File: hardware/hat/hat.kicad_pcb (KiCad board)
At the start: 4 copper layers, 65 x 56 mm, 82 parts, among them J1 GPIO, J2 Uart, J3 LineIn, J4 LineOut, J5 Headphone, U1 CAT24C256, U2 TPS7A20xxxDBV, U3 Oled, U4 MAX98089ETN_T, Y1 12.288MHz

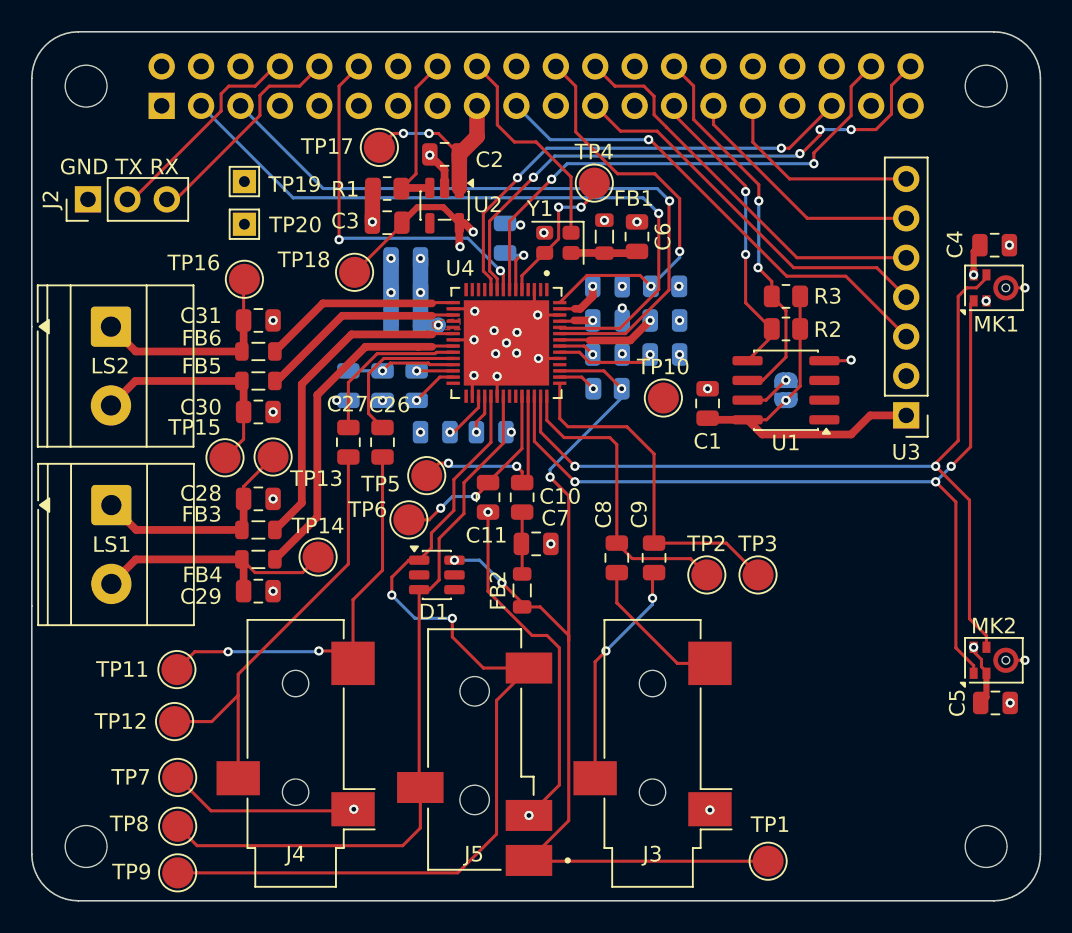
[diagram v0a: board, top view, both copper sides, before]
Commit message: make hat 100 x sheetnum
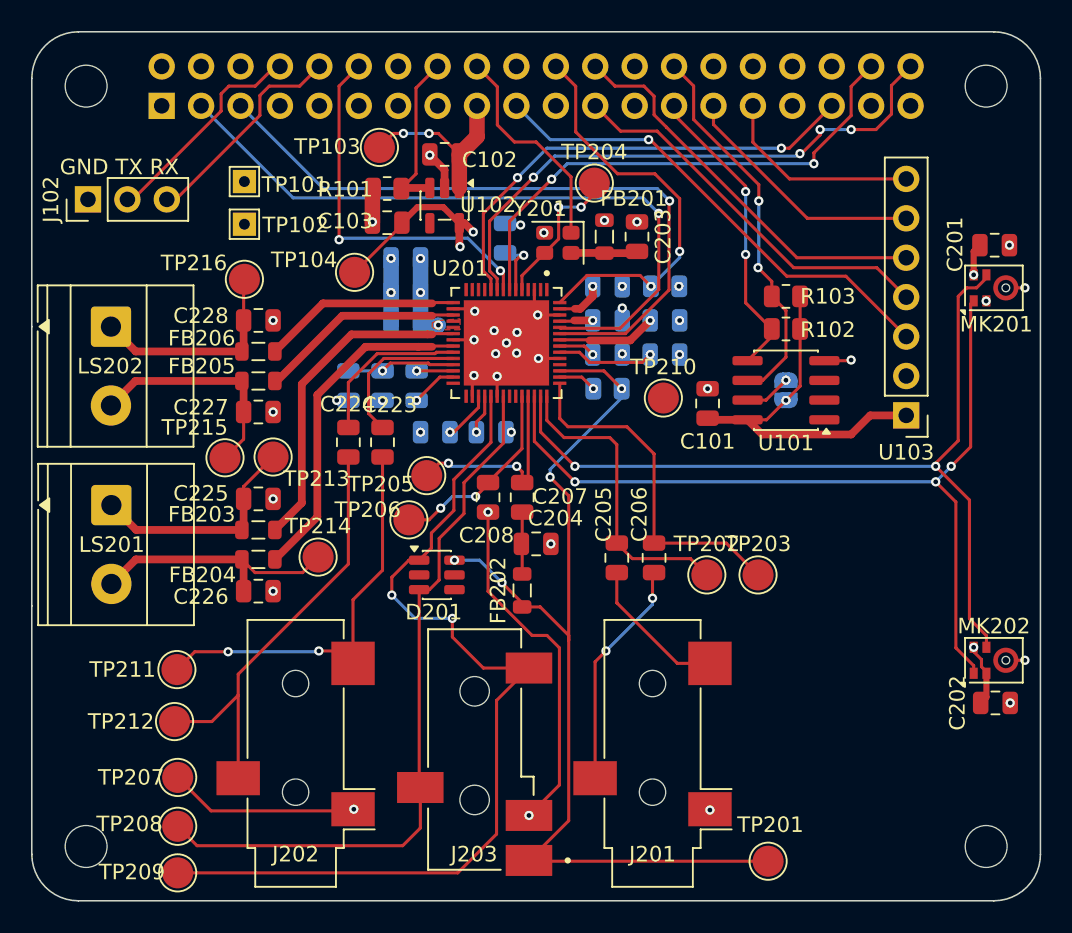
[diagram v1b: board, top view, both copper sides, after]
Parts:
- renumbered C1 to C101, C2 to C102, C3 to C103, C4 to C201, C5 to C202, C6 to C203, C7 to C204, C8 to C205, C9 to C206, C10 to C207, C11 to C208, C12 to C209, C13 to C210, C14 to C211, C15 to C212, C16 to C213, C17 to C214, C18 to C215, C19 to C216, C20 to C217, C21 to C218, C22 to C219, C23 to C220, C24 to C221, C25 to C222, C26 to C223, C27 to C224, C28 to C225, C29 to C226, C30 to C227, C31 to C228, D1 to D201, FB1 to FB201, FB2 to FB202, FB3 to FB203, FB4 to FB204, FB5 to FB205, FB6 to FB206, J1 to J101, J2 to J102, J3 to J201, J4 to J202, J5 to J203, JP1 to JP101, LS1 to LS201, LS2 to LS202, MK1 to MK201, MK2 to MK202, R1 to R101, R2 to R102, R3 to R103, R4 to R201, R5 to R202, TP19 to TP101, TP20 to TP102, TP17 to TP103, TP18 to TP104, TP1 to TP201, TP2 to TP202, TP3 to TP203, TP4 to TP204, TP5 to TP205, TP6 to TP206, TP7 to TP207, TP8 to TP208, TP9 to TP209, TP10 to TP210, TP11 to TP211, TP12 to TP212, TP13 to TP213, TP14 to TP214, TP15 to TP215, TP16 to TP216, U1 to U101, U2 to U102, U3 to U103, U4 to U201, Y1 to Y201

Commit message: move ldo into audio sheet
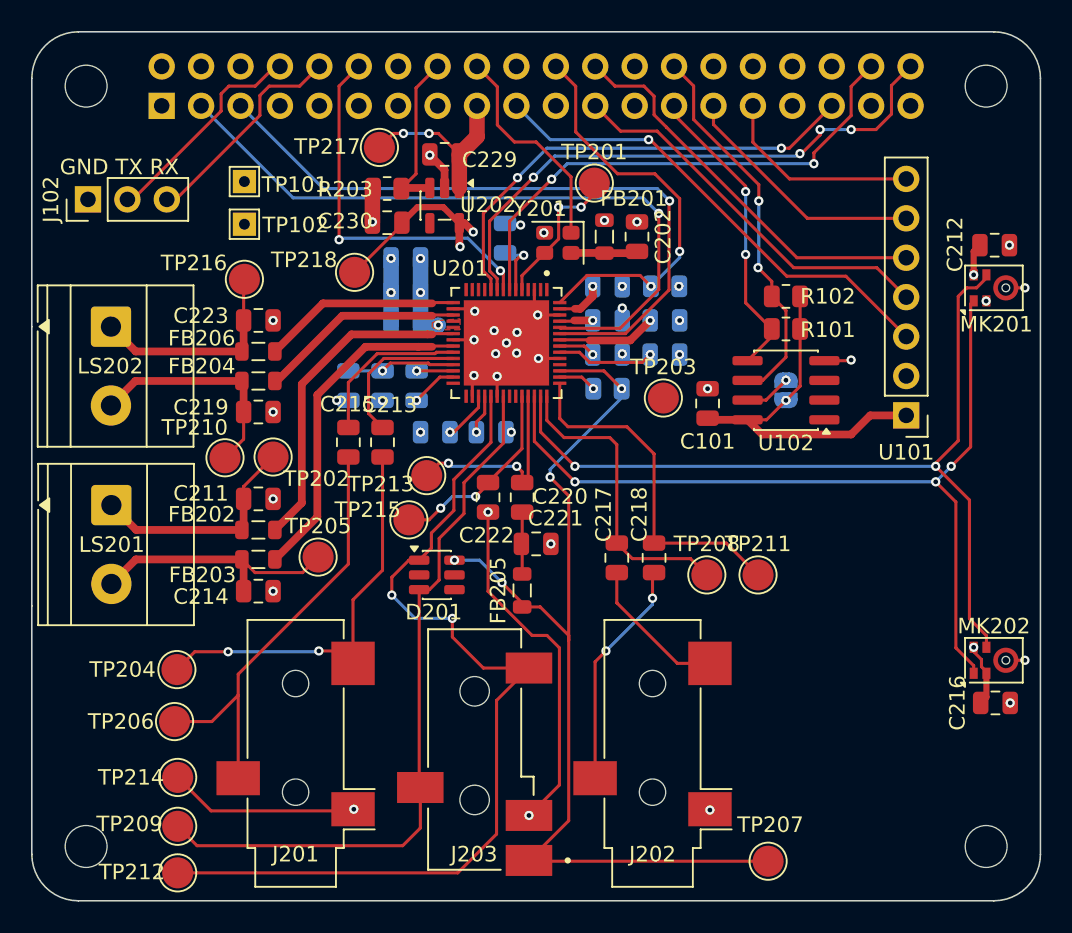
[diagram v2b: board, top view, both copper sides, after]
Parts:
- renumbered C214 to C201, C203 to C202, C211 to C203, C209 to C204, C210 to C205, C212 to C206, C213 to C207, C215 to C208, C218 to C209, C220 to C210, C225 to C211, C201 to C212, C223 to C213, C226 to C214, C224 to C215, C202 to C216, C205 to C217, C206 to C218, C227 to C219, C207 to C220, C204 to C221, C208 to C222, C228 to C223, C221 to C224, C222 to C225, C216 to C226, C217 to C227, C219 to C228, C102 to C229, C103 to C230, FB203 to FB202, FB204 to FB203, FB205 to FB204, FB202 to FB205, J202 to J201, J201 to J202, R102 to R101, R103 to R102, R101 to R203, TP204 to TP201, TP213 to TP202, TP210 to TP203, TP211 to TP204, TP214 to TP205, TP212 to TP206, TP201 to TP207, TP202 to TP208, TP208 to TP209, TP215 to TP210, TP203 to TP211, TP209 to TP212, TP205 to TP213, TP207 to TP214, TP206 to TP215, TP103 to TP217, TP104 to TP218, U103 to U101, U101 to U102, U102 to U202
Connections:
- J101 pad 16: /1V8_EN -> /GPIO23
- R203 pad 1: /1V8_EN -> /codec/1V8_EN
- U202 pad 3: /1V8_EN -> /codec/1V8_EN
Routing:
- net /1V8_EN: track 10.7 -> 0.00 mm
- net (no net): track 0.00 -> 10.7 mm

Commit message: use H label for 1v8en
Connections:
- R203 pad 1: /codec/1V8_EN -> /GPIO23
- U202 pad 3: /codec/1V8_EN -> /GPIO23
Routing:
- net /GPIO23: track 0.00 -> 10.7 mm
- net (no net): track 10.7 -> 0.00 mm
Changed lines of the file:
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@@
 			(layers "F.Cu" "F.Mask" "F.Paste")
 			(roundrect_rratio 0.243902)
-			(net "/codec/1V8_EN")
+			(net "/GPIO23")
 			(pintype "passive")
 		)
@@
 			(layers "F.Cu" "F.Mask" "F.Paste")
 			(roundrect_rratio 0.25)
-			(net "/codec/1V8_EN")
+			(net "/GPIO23")
 			(pinfunction "EN_3")
 			(pintype "input")
@@
 	)
 	(segment
-		(start 124.76 53.1525)
-		(end 124.76 47.62)
-		(width 0.2)
-		(layer "F.Cu")
-		(net "")
-	)
-	(segment
-		(start 123.85 54.0625)
-		(end 123.8125 54.1)
-		(width 0.5)
-		(layer "F.Cu")
-		(net "")
-	)
-	(segment
-		(start 124.76 47.62)
-		(end 126.15 46.23)
-		(width 0.2)
-		(layer "F.Cu")
-		(net "")
-	)
-	(segment
-		(start 123.8125 54.1)
-		(end 124.76 53.1525)
-		(width 0.2)
-		(layer "F.Cu")
-		(net "")
-	)
-	(segment
-		(start 125.65 54.0625)
-		(end 123.85 54.0625)
-		(width 0.5)
-		(layer "F.Cu")
-		(net "")
-	)
-	(segment
 		(start 134.75 56.95)
 		(end 134.75 53.35)
@@
 	)
 	(segment
+		(start 124.76 53.1525)
+		(end 124.76 47.62)
+		(width 0.2)
+		(layer "F.Cu")
+		(net "/GPIO23")
+	)
+	(segment
+		(start 123.85 54.0625)
+		(end 123.8125 54.1)
+		(width 0.5)
+		(layer "F.Cu")
+		(net "/GPIO23")
+	)
+	(segment
+		(start 124.76 47.62)
+		(end 126.15 46.23)
+		(width 0.2)
+		(layer "F.Cu")
+		(net "/GPIO23")
+	)
+	(segment
+		(start 123.8125 54.1)
+		(end 124.76 53.1525)
+		(width 0.2)
+		(layer "F.Cu")
+		(net "/GPIO23")
+	)
+	(segment
+		(start 125.65 54.0625)
+		(end 123.85 54.0625)
+		(width 0.5)
+		(layer "F.Cu")
+		(net "/GPIO23")
+	)
+	(segment

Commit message: delete FB and cap from hat
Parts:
- removed the C221 at (132.5, 77.0)
- removed the FB205 at (131.6, 80.0)
- renumbered C222 to C221, C223 to C222, C224 to C223, C225 to C224, C226 to C225, C227 to C226, C228 to C227, C229 to C228, C230 to C229, FB206 to FB205
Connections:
- C220 pad 1: Net-(C220-Pad1) -> /codec/JackS
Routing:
- net /codec/JackS: track 63.6 -> 69.2 mm
- net Net-(C220-Pad1): track 4.03 -> 0.00 mm
